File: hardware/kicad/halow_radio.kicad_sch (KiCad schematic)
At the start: 0 parts

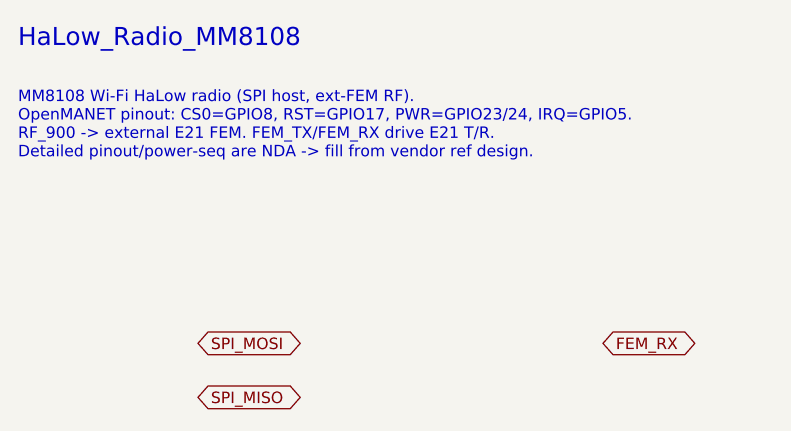
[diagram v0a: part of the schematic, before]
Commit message: Deepen design to component level + fix EEPROM power rail
- Fix: HAT ID EEPROM (U6) now powered from Pi header 3V3 (3V3_PI, pin 1)
  so it is readable at boot before the HAT's own 3V3 comes up (was
  incorrectly on the HAT 3V3 regulator).
- Add docs/SCHEMATIC.md: component-level subcircuits for every block
  (refdes + values + nets) — buck-boost/3V3 FB dividers, MM8108 SPI
  termination/pulls, E21 RF DC-blocks/attenuator pad/T-R pulldowns,
  NEO-M9N active-antenna bias via VCC_RF, ID EEPROM (WP default).
- Add docs/BRINGUP.md: stage-gated power-on + RF test plan (don't key
  the 1W PA until rails/drive-level/FEM-timing verified).
- Add GNSS VCC_RF antenna bias + +3V3_GNSS ferrite to the net list.
- Enrich KiCad sub-sheets with per-block refdes notes and the new nets;
  regenerate scaffold (KiCad 10 format, S-expression balance re-checked).
- BOM: concrete passives (RF DC-blocks, attenuator pad, ferrite, TVS,
  FB dividers, WP jumper).

https://claude.ai/code/session_015nkkW85U3sPf5mcvrsMw7T
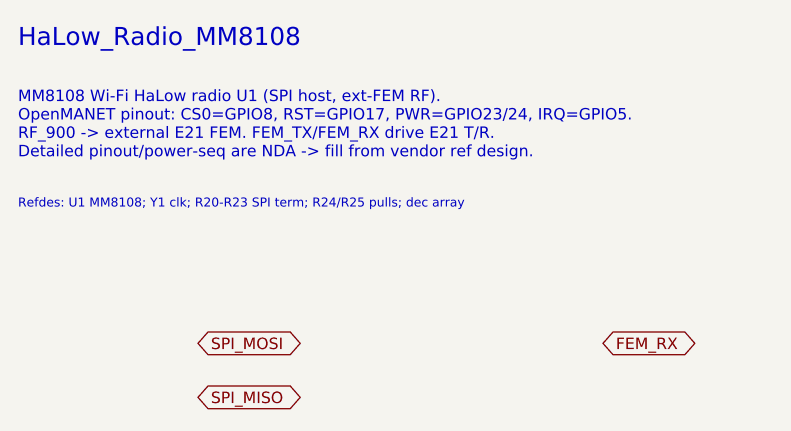
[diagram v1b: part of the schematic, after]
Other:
- note added: "MM8108 Wi-Fi HaLow radio U1 (SPI host, ext-FEM RF). OpenMANET pinout: CS0=GPIO8, RST=GPIO17, PWR=GPIO23/24, IRQ=GPIO5. RF_900 -> external E21 FEM. FEM_TX/FEM_RX drive E21 T/R. Detailed pinout/power-seq are NDA -> fill from vendor ref design."
- note added: "Refdes: U1 MM8108; Y1 clk; R20-R23 SPI term; R24/R25 pulls; dec array"
- note removed: "MM8108 Wi-Fi HaLow radio (SPI host, ext-FEM RF). OpenMANET pinout: CS0=GPIO8, RST=GPIO17, PWR=GPIO23/24, IRQ=GPIO5. RF_900 -> external E21 FEM. FEM_TX/FEM_RX drive E21 T/R. Detailed pinout/power-seq are NDA -> fill from vendor ref design."
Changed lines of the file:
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@@
 	(paper "A4")
 	(text "HaLow_Radio_MM8108" (exclude_from_sim no) (at 20 15 0) (effects (font (size 2 2) (thickness 0.3)) (justify left top)))
-	(text "MM8108 Wi-Fi HaLow radio (SPI host, ext-FEM RF).\nOpenMANET pinout: CS0=GPIO8, RST=GPIO17, PWR=GPIO23/24, IRQ=GPIO5.\nRF_900 -> external E21 FEM. FEM_TX/FEM_RX drive E21 T/R.\nDetailed pinout/power-seq are NDA -> fill from vendor ref design." (exclude_from_sim no) (at 20 22 0) (effects (font (size 1.27 1.27)) (justify left top)))
+	(text "MM8108 Wi-Fi HaLow radio U1 (SPI host, ext-FEM RF).\nOpenMANET pinout: CS0=GPIO8, RST=GPIO17, PWR=GPIO23/24, IRQ=GPIO5.\nRF_900 -> external E21 FEM. FEM_TX/FEM_RX drive E21 T/R.\nDetailed pinout/power-seq are NDA -> fill from vendor ref design." (exclude_from_sim no) (at 20 22 0) (effects (font (size 1.27 1.27)) (justify left top)))
+	(text "Refdes: U1 MM8108; Y1 clk; R20-R23 SPI term; R24/R25 pulls; dec array" (exclude_from_sim no) (at 20 34 0) (effects (font (size 1.0 1.0)) (justify left top)))
 	(global_label "SPI_MOSI" (shape bidirectional) (at 40 50 0) (fields_autoplaced yes) (effects (font (size 1.27 1.27)) (justify left)))
 	(global_label "SPI_MISO" (shape bidirectional) (at 40 56 0) (fields_autoplaced yes) (effects (font (size 1.27 1.27)) (justify left)))

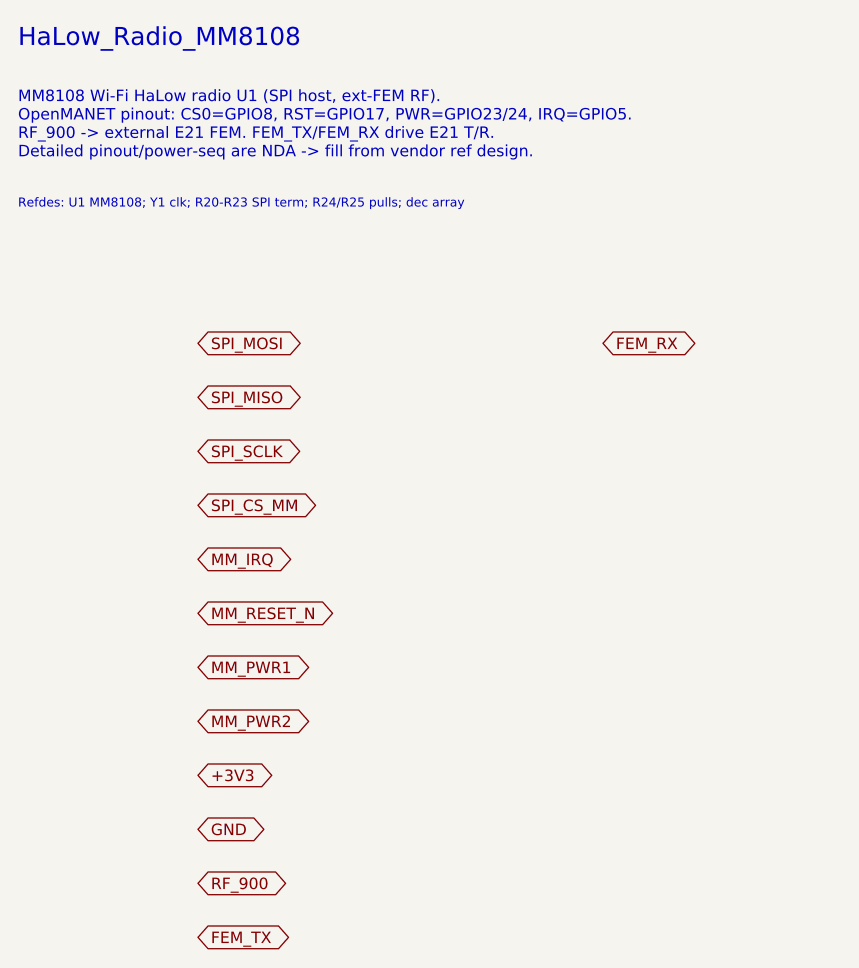
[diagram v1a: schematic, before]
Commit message: Add gap-analysis components (datasheet-grounded) + RTC
Read the uploaded datasheets (MM8108-MF15457, E21-900G30S, NEO-M9N-00B)
and resolved the component gaps:

- #1/#2 RESOLVED by the module: MF15457 is self-contained (internal
  clock+PMU+PA); only needs VBAT/VBAT_TX/VDDIO 3.0-3.6 V. No external SoC
  inductors, 1V8/1V2 rails, or TCXO.
- VPA fixed at 5.0 V (E21 needs 4.75-5.25 V, ~620 mA TX, +20 dBm in ->
  +30 dBm out, 12 dB gain). Real pinouts wired (module 38-pin; E21
  pin6=PIN xcvr, pin9=ANT).
- Architecture finding: module has integrated PA + single ANT pin and NO
  hardware T/R FEM line. External E21 now needs (a) ~3-5 dB drive pad,
  (b) T/R control via module GPIO0/1 toggled by OpenMANET FW (or RF-sense
  auto-T/R fallback), and (c) end-product recertification at +30 dBm.

Added components:
- N3 900 MHz harmonic LPF (FL2); N4 inrush soft-start load switch (U10);
  N5 supervisor (U11); N6 radio-rail load switch (U12, OpenMANET
  power-gpios); N7 RF shields; N8 GNSS antenna ESD (D8); N9 status LEDs;
  N10 E21 thermal relief.
- RTC: RV-3028-C7 (U13) on I2C1 0x52 with a soldered rechargeable cell
  (BT1, trickle-charged) per request; added to the device-tree overlay.
- Declined per request: debug UART/JTAG pads, test points.

Updated docs (new COMPONENTS_GAP.md; DECISIONS B1-B9; SCHEMATIC; BOM;
POWER budget), netlist, overlay, and regenerated the KiCad 10 scaffold
with the new nets. Committed the vendor datasheets under hardware/.

https://claude.ai/code/session_015nkkW85U3sPf5mcvrsMw7T
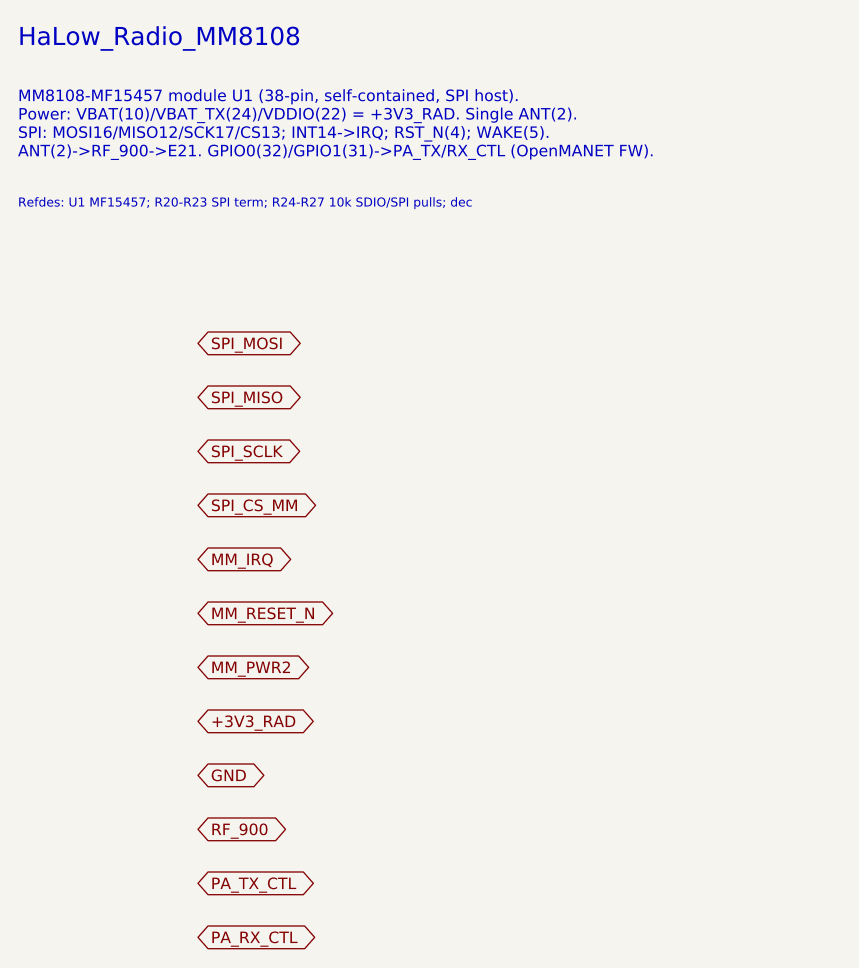
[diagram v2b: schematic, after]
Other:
- note added: "MM8108-MF15457 module U1 (38-pin, self-contained, SPI host). Power: VBAT(10)/VBAT_TX(24)/VDDIO(22) = +3V3_RAD. Single ANT(2). SPI: MOSI16/MISO12/SCK17/CS13; INT14->IRQ; RST_N(4); WAKE(5). ANT(2)->RF_900->E21. GPIO0(32)/GPIO1(31)->PA_TX/RX_CTL (OpenMANET FW)."
- note added: "Refdes: U1 MF15457; R20-R23 SPI term; R24-R27 10k SDIO/SPI pulls; dec"
- note removed: "MM8108 Wi-Fi HaLow radio U1 (SPI host, ext-FEM RF). OpenMANET pinout: CS0=GPIO8, RST=GPIO17, PWR=GPIO23/24, IRQ=GPIO5. RF_900 -> external E21 FEM. FEM_TX/FEM_RX drive E21 T/R. Detailed pinout/power-seq are NDA -> fill from vendor ref design."
- note removed: "Refdes: U1 MM8108; Y1 clk; R20-R23 SPI term; R24/R25 pulls; dec array"
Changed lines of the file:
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@@
 	(paper "A4")
 	(text "HaLow_Radio_MM8108" (exclude_from_sim no) (at 20 15 0) (effects (font (size 2 2) (thickness 0.3)) (justify left top)))
-	(text "MM8108 Wi-Fi HaLow radio U1 (SPI host, ext-FEM RF).\nOpenMANET pinout: CS0=GPIO8, RST=GPIO17, PWR=GPIO23/24, IRQ=GPIO5.\nRF_900 -> external E21 FEM. FEM_TX/FEM_RX drive E21 T/R.\nDetailed pinout/power-seq are NDA -> fill from vendor ref design." (exclude_from_sim no) (at 20 22 0) (effects (font (size 1.27 1.27)) (justify left top)))
-	(text "Refdes: U1 MM8108; Y1 clk; R20-R23 SPI term; R24/R25 pulls; dec array" (exclude_from_sim no) (at 20 34 0) (effects (font (size 1.0 1.0)) (justify left top)))
+	(text "MM8108-MF15457 module U1 (38-pin, self-contained, SPI host).\nPower: VBAT(10)/VBAT_TX(24)/VDDIO(22) = +3V3_RAD. Single ANT(2).\nSPI: MOSI16/MISO12/SCK17/CS13; INT14->IRQ; RST_N(4); WAKE(5).\nANT(2)->RF_900->E21. GPIO0(32)/GPIO1(31)->PA_TX/RX_CTL (OpenMANET FW)." (exclude_from_sim no) (at 20 22 0) (effects (font (size 1.27 1.27)) (justify left top)))
+	(text "Refdes: U1 MF15457; R20-R23 SPI term; R24-R27 10k SDIO/SPI pulls; dec" (exclude_from_sim no) (at 20 34 0) (effects (font (size 1.0 1.0)) (justify left top)))
 	(global_label "SPI_MOSI" (shape bidirectional) (at 40 50 0) (fields_autoplaced yes) (effects (font (size 1.27 1.27)) (justify left)))
 	(global_label "SPI_MISO" (shape bidirectional) (at 40 56 0) (fields_autoplaced yes) (effects (font (size 1.27 1.27)) (justify left)))
@@
 	(global_label "MM_IRQ" (shape bidirectional) (at 40 74 0) (fields_autoplaced yes) (effects (font (size 1.27 1.27)) (justify left)))
 	(global_label "MM_RESET_N" (shape bidirectional) (at 40 80 0) (fields_autoplaced yes) (effects (font (size 1.27 1.27)) (justify left)))
-	(global_label "MM_PWR1" (shape bidirectional) (at 40 86 0) (fields_autoplaced yes) (effects (font (size 1.27 1.27)) (justify left)))
-	(global_label "MM_PWR2" (shape bidirectional) (at 40 92 0) (fields_autoplaced yes) (effects (font (size 1.27 1.27)) (justify left)))
-	(global_label "+3V3" (shape bidirectional) (at 40 98 0) (fields_autoplaced yes) (effects (font (size 1.27 1.27)) (justify left)))
-	(global_label "GND" (shape bidirectional) (at 40 104 0) (fields_autoplaced yes) (effects (font (size 1.27 1.27)) (justify left)))
-	(global_label "RF_900" (shape bidirectional) (at 40 110 0) (fields_autoplaced yes) (effects (font (size 1.27 1.27)) (justify left)))
-	(global_label "FEM_TX" (shape bidirectional) (at 40 116 0) (fields_autoplaced yes) (effects (font (size 1.27 1.27)) (justify left)))
-	(global_label "FEM_RX" (shape bidirectional) (at 85 50 0) (fields_autoplaced yes) (effects (font (size 1.27 1.27)) (justify left)))
+	(global_label "MM_PWR2" (shape bidirectional) (at 40 86 0) (fields_autoplaced yes) (effects (font (size 1.27 1.27)) (justify left)))
+	(global_label "+3V3_RAD" (shape bidirectional) (at 40 92 0) (fields_autoplaced yes) (effects (font (size 1.27 1.27)) (justify left)))
+	(global_label "GND" (shape bidirectional) (at 40 98 0) (fields_autoplaced yes) (effects (font (size 1.27 1.27)) (justify left)))
+	(global_label "RF_900" (shape bidirectional) (at 40 104 0) (fields_autoplaced yes) (effects (font (size 1.27 1.27)) (justify left)))
+	(global_label "PA_TX_CTL" (shape bidirectional) (at 40 110 0) (fields_autoplaced yes) (effects (font (size 1.27 1.27)) (justify left)))
+	(global_label "PA_RX_CTL" (shape bidirectional) (at 40 116 0) (fields_autoplaced yes) (effects (font (size 1.27 1.27)) (justify left)))
 )

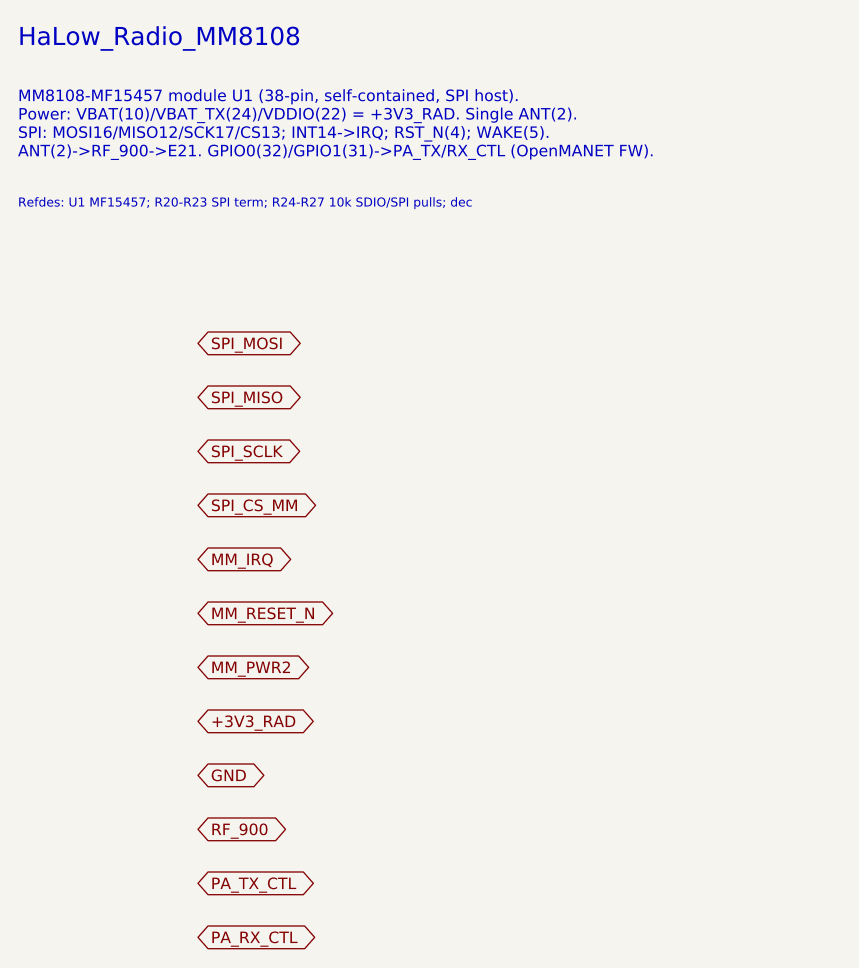
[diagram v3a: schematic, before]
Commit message: Pivot to MM8108-M20 primary / MF15457 fallback; retire external E21
Per the decision to make the MM8108-M20 the primary radio (with MF15457
as the build-today fallback) and retire the external E21 PA path:

Design:
- One radio site fed by the shared SPI/control nets accepts either module.
- Removed the E21 PA, 5V buck-boost (VPA), harmonic LPF, drive pad, T/R
  control, RF-sense VOX, and RF bypass. Both modules drive the antenna
  directly (M20 = integrated 28.5 dBm PA + 902-928 SAW, certified;
  MF15457 = ~27 dBm). Power collapses to a single 3V3 rail.
- Header GPIO4/6 (old FEM fallback) revert to spares; GPIO12/13 drive the
  status LEDs.
- M20 pinout/power/footprint held at placeholder pending its datasheet
  (B12); MF15457 pin-level detail stays the concrete baseline.

Docs updated: DECISIONS (A3 superseded, B11/B12 added, B2-B5/B10 retired,
new radio-options table + order), DESIGN, SCHEMATIC, POWER, RF, BOM,
INTERFACES, COMPONENTS_GAP, LINK_BUDGET, FIRMWARE_PA, BRINGUP, MECHANICAL,
README. Netlist, KiCad scaffold (sheets/silk/root note), and the OpenMANET
overlay/README updated to match. Scaffold regenerated and validated.

https://claude.ai/code/session_015nkkW85U3sPf5mcvrsMw7T
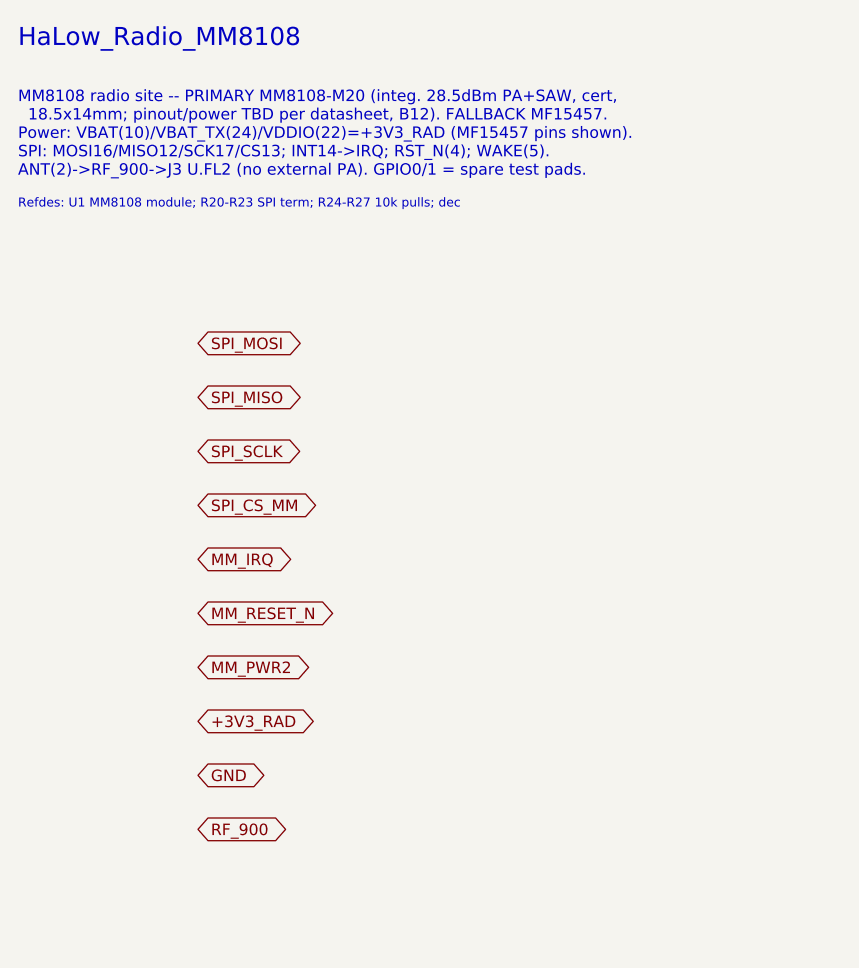
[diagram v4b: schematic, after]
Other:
- note added: "MM8108 radio site -- PRIMARY MM8108-M20 (integ. 28.5dBm PA+SAW, cert, 18.5x14mm; pinout/power TBD per datasheet, B12). FALLBACK MF15457. Power: VBAT(10)/VBAT_TX(24)/VDDIO(22)=+3V3_RAD (MF15457 pins shown). SPI: MOSI16/MISO12/SCK17/CS13; INT14->IRQ; RST_N(4); WAKE(5). ANT(2)->RF_900->J3 U.FL2 (no external PA). GPIO0/1 = spare test pads."
- note added: "Refdes: U1 MM8108 module; R20-R23 SPI term; R24-R27 10k pulls; dec"
- note removed: "MM8108-MF15457 module U1 (38-pin, self-contained, SPI host). Power: VBAT(10)/VBAT_TX(24)/VDDIO(22) = +3V3_RAD. Single ANT(2). SPI: MOSI16/MISO12/SCK17/CS13; INT14->IRQ; RST_N(4); WAKE(5). ANT(2)->RF_900->E21. GPIO0(32)/GPIO1(31)->PA_TX/RX_CTL (OpenMANET FW)."
- note removed: "Refdes: U1 MF15457; R20-R23 SPI term; R24-R27 10k SDIO/SPI pulls; dec"
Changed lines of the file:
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@@
 	(paper "A4")
 	(text "HaLow_Radio_MM8108" (exclude_from_sim no) (at 20 15 0) (effects (font (size 2 2) (thickness 0.3)) (justify left top)))
-	(text "MM8108-MF15457 module U1 (38-pin, self-contained, SPI host).\nPower: VBAT(10)/VBAT_TX(24)/VDDIO(22) = +3V3_RAD. Single ANT(2).\nSPI: MOSI16/MISO12/SCK17/CS13; INT14->IRQ; RST_N(4); WAKE(5).\nANT(2)->RF_900->E21. GPIO0(32)/GPIO1(31)->PA_TX/RX_CTL (OpenMANET FW)." (exclude_from_sim no) (at 20 22 0) (effects (font (size 1.27 1.27)) (justify left top)))
-	(text "Refdes: U1 MF15457; R20-R23 SPI term; R24-R27 10k SDIO/SPI pulls; dec" (exclude_from_sim no) (at 20 34 0) (effects (font (size 1.0 1.0)) (justify left top)))
+	(text "MM8108 radio site -- PRIMARY MM8108-M20 (integ. 28.5dBm PA+SAW, cert,\n  18.5x14mm; pinout/power TBD per datasheet, B12). FALLBACK MF15457.\nPower: VBAT(10)/VBAT_TX(24)/VDDIO(22)=+3V3_RAD (MF15457 pins shown).\nSPI: MOSI16/MISO12/SCK17/CS13; INT14->IRQ; RST_N(4); WAKE(5).\nANT(2)->RF_900->J3 U.FL2 (no external PA). GPIO0/1 = spare test pads." (exclude_from_sim no) (at 20 22 0) (effects (font (size 1.27 1.27)) (justify left top)))
+	(text "Refdes: U1 MM8108 module; R20-R23 SPI term; R24-R27 10k pulls; dec" (exclude_from_sim no) (at 20 34 0) (effects (font (size 1.0 1.0)) (justify left top)))
 	(global_label "SPI_MOSI" (shape bidirectional) (at 40 50 0) (fields_autoplaced yes) (effects (font (size 1.27 1.27)) (justify left)))
 	(global_label "SPI_MISO" (shape bidirectional) (at 40 56 0) (fields_autoplaced yes) (effects (font (size 1.27 1.27)) (justify left)))
@@
 	(global_label "GND" (shape bidirectional) (at 40 98 0) (fields_autoplaced yes) (effects (font (size 1.27 1.27)) (justify left)))
 	(global_label "RF_900" (shape bidirectional) (at 40 104 0) (fields_autoplaced yes) (effects (font (size 1.27 1.27)) (justify left)))
-	(global_label "PA_TX_CTL" (shape bidirectional) (at 40 110 0) (fields_autoplaced yes) (effects (font (size 1.27 1.27)) (justify left)))
-	(global_label "PA_RX_CTL" (shape bidirectional) (at 40 116 0) (fields_autoplaced yes) (effects (font (size 1.27 1.27)) (justify left)))
 )
